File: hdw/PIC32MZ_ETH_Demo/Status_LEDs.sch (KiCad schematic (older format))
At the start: 30 parts

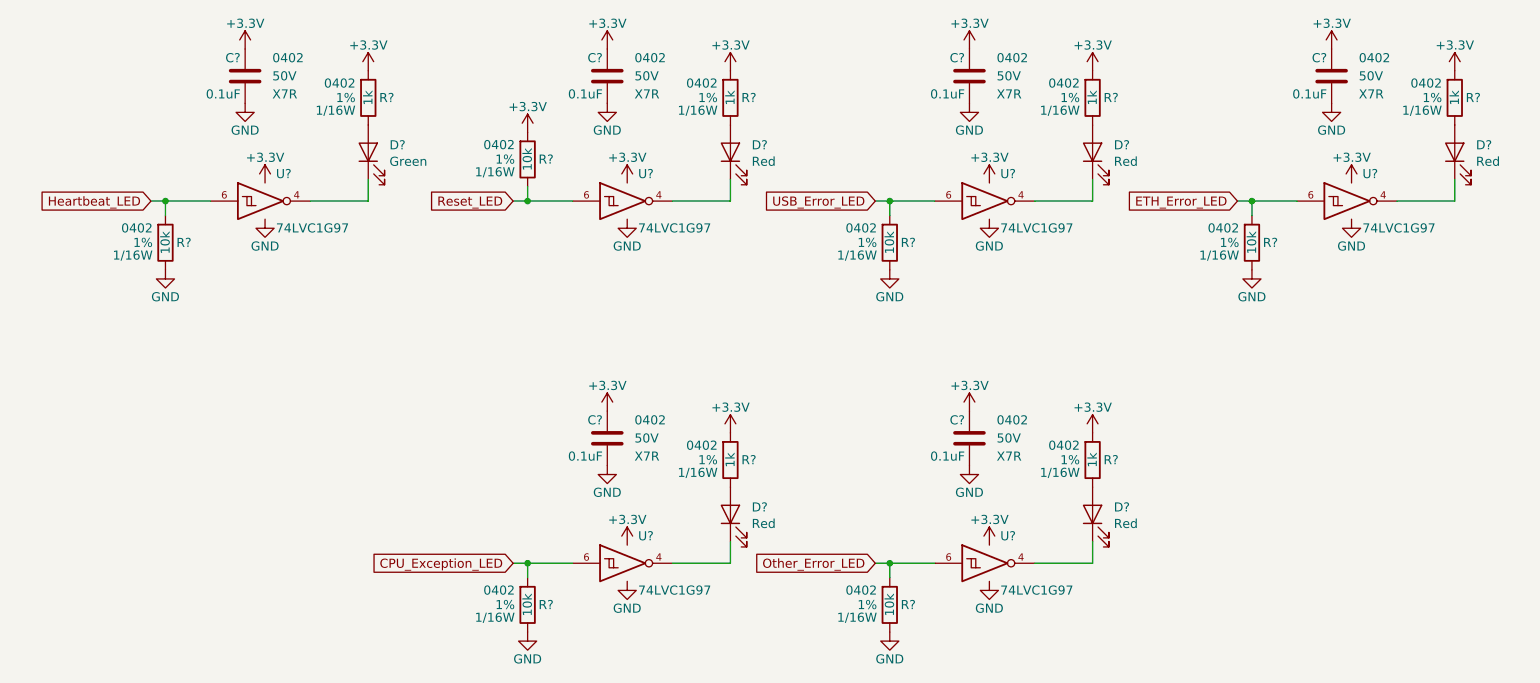
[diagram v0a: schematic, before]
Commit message: More schematic tweaks, followed PHY design guide
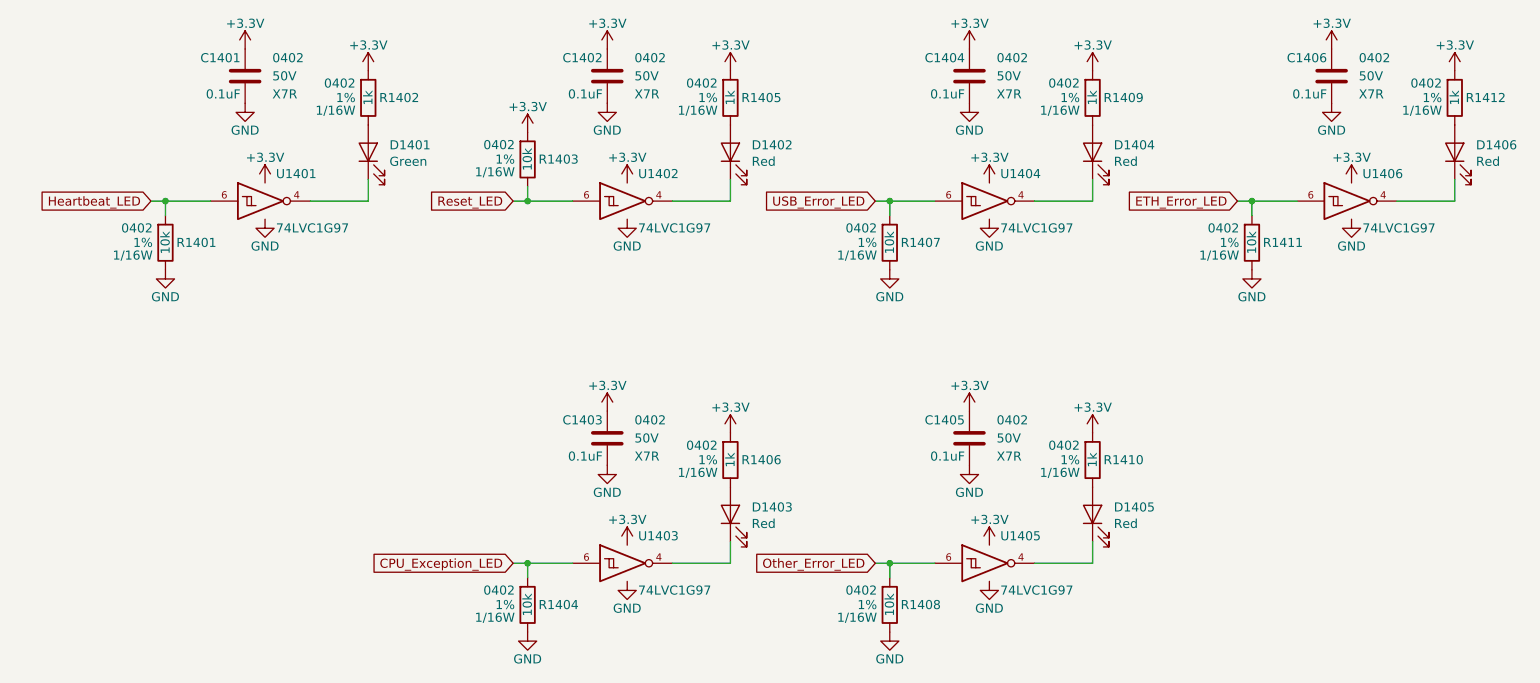
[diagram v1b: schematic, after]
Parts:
- gave numbers to parts that had none: 30

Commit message: Populated digi-key pn's
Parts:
- C1401, C1402, C1403, C1404, C1405, C1406: Digi-Key PN (none) -> 490-10701-1-ND
- D1401: footprint LEDs:LED_0603 -> LEDs:LED_0402; Digi-Key PN (none) -> 1497-1219-1-ND
- D1402, D1403, D1404, D1405, D1406: footprint LEDs:LED_0603 -> LEDs:LED_0402; Digi-Key PN (none) -> 1497-1174-1-ND
- R1401, R1403, R1404, R1407, R1408, R1411: Digi-Key PN (none) -> RMCF0402FT10K0CT-ND
- R1402, R1405, R1406, R1409, R1410, R1412: Digi-Key PN (none) -> 541-1.00KLCT-ND
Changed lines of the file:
@@
 F 2 "Capacitors_SMD:C_0402" H 2328 1380 50  0001 C CNN
 F 3 "" H 2315 1630 50  0001 C CNN
-F 4 "" H 2715 2030 60  0001 C CNN "Digi-Key PN"
+F 4 "490-10701-1-ND" H 2715 2030 60  0001 C CNN "Digi-Key PN"
 F 5 "0402" H 2140 1630 50  0000 R CNN "display_footprint"
 F 6 "50V" H 2140 1530 50  0000 R CNN "Voltage"
@@
 F 0 "D1401" V 3009 1833 50  0000 R CNN
 F 1 "Green" V 2918 1833 50  0000 R CNN
-F 2 "LEDs:LED_0603" H 2970 1950 50  0001 C CNN
+F 2 "LEDs:LED_0402" H 2970 1950 50  0001 C CNN
 F 3 "~" H 2970 1950 50  0001 C CNN
-F 4 "" H -2190 -4370 50  0001 C CNN "Digi-Key PN"
+F 4 "1497-1219-1-ND" H -2190 -4370 50  0001 C CNN "Digi-Key PN"
 	1    2970 1950
 	0    -1   -1   0
@@
 F 5 "1%" H 3040 1650 50  0000 L CNN "Tolerance"
 F 6 "1/16W" H 3040 1580 50  0000 L CNN "Wattage"
-F 7 "" H 3270 2050 60  0001 C CNN "Digi-Key PN"
+F 7 "541-1.00KLCT-ND" H 3270 2050 60  0001 C CNN "Digi-Key PN"
 	1    2970 1650
 	-1   0    0    -1
@@
 F 5 "1%" H 1920 2450 50  0000 L CNN "Tolerance"
 F 6 "1/16W" H 1920 2380 50  0000 L CNN "Wattage"
-F 7 "" H 1850 2450 50  0001 C CNN "Digi-Key PN"
+F 7 "RMCF0402FT10K0CT-ND" H 1850 2450 50  0001 C CNN "Digi-Key PN"
 	1    1850 2450
 	-1   0    0    -1
@@
 F 2 "Capacitors_SMD:C_0402" H 4328 1380 50  0001 C CNN
 F 3 "" H 4315 1630 50  0001 C CNN
-F 4 "" H 4715 2030 60  0001 C CNN "Digi-Key PN"
+F 4 "490-10701-1-ND" H 4715 2030 60  0001 C CNN "Digi-Key PN"
 F 5 "0402" H 4140 1630 50  0000 R CNN "display_footprint"
 F 6 "50V" H 4140 1530 50  0000 R CNN "Voltage"
@@
 F 0 "D1402" V 5009 1833 50  0000 R CNN
 F 1 "Red" V 4918 1833 50  0000 R CNN
-F 2 "LEDs:LED_0603" H 4970 1950 50  0001 C CNN
+F 2 "LEDs:LED_0402" H 4970 1950 50  0001 C CNN
 F 3 "~" H 4970 1950 50  0001 C CNN
-F 4 "" H 4970 1950 50  0001 C CNN "Digi-Key PN"
+F 4 "1497-1174-1-ND" H 4970 1950 50  0001 C CNN "Digi-Key PN"
 	1    4970 1950
 	0    -1   -1   0
@@
 F 5 "1%" H 5040 1650 50  0000 L CNN "Tolerance"
 F 6 "1/16W" H 5040 1580 50  0000 L CNN "Wattage"
-F 7 "" H 5270 2050 60  0001 C CNN "Digi-Key PN"
+F 7 "541-1.00KLCT-ND" H 5270 2050 60  0001 C CNN "Digi-Key PN"
 	1    4970 1650
 	-1   0    0    -1
@@
 F 5 "1%" H 3920 1990 50  0000 L CNN "Tolerance"
 F 6 "1/16W" H 3920 1920 50  0000 L CNN "Wattage"
-F 7 "" H 3850 1990 50  0001 C CNN "Digi-Key PN"
+F 7 "RMCF0402FT10K0CT-ND" H 3850 1990 50  0001 C CNN "Digi-Key PN"
 	1    3850 1990
 	-1   0    0    -1
@@
 F 2 "Capacitors_SMD:C_0402" H 6328 1380 50  0001 C CNN
 F 3 "" H 6315 1630 50  0001 C CNN
-F 4 "" H 6715 2030 60  0001 C CNN "Digi-Key PN"
+F 4 "490-10701-1-ND" H 6715 2030 60  0001 C CNN "Digi-Key PN"
 F 5 "0402" H 6140 1630 50  0000 R CNN "display_footprint"
 F 6 "50V" H 6140 1530 50  0000 R CNN "Voltage"
@@
 F 5 "1%" H 7040 1650 50  0000 L CNN "Tolerance"
 F 6 "1/16W" H 7040 1580 50  0000 L CNN "Wattage"
-F 7 "" H 7270 2050 60  0001 C CNN "Digi-Key PN"
+F 7 "541-1.00KLCT-ND" H 7270 2050 60  0001 C CNN "Digi-Key PN"
 	1    6970 1650
 	-1   0    0    -1
@@
 F 5 "1%" H 5920 2450 50  0000 L CNN "Tolerance"
 F 6 "1/16W" H 5920 2380 50  0000 L CNN "Wattage"
-F 7 "" H 5850 2450 50  0001 C CNN "Digi-Key PN"
+F 7 "RMCF0402FT10K0CT-ND" H 5850 2450 50  0001 C CNN "Digi-Key PN"
 	1    5850 2450
 	-1   0    0    -1
@@
 F 0 "D1404" V 7009 1833 50  0000 R CNN
 F 1 "Red" V 6918 1833 50  0000 R CNN
-F 2 "LEDs:LED_0603" H 6970 1950 50  0001 C CNN
+F 2 "LEDs:LED_0402" H 6970 1950 50  0001 C CNN
 F 3 "~" H 6970 1950 50  0001 C CNN
-F 4 "" H 6970 1950 50  0001 C CNN "Digi-Key PN"
+F 4 "1497-1174-1-ND" H 6970 1950 50  0001 C CNN "Digi-Key PN"
 	1    6970 1950
 	0    -1   -1   0
@@
 F 2 "Capacitors_SMD:C_0402" H 8328 1380 50  0001 C CNN
 F 3 "" H 8315 1630 50  0001 C CNN
-F 4 "" H 8715 2030 60  0001 C CNN "Digi-Key PN"
+F 4 "490-10701-1-ND" H 8715 2030 60  0001 C CNN "Digi-Key PN"
 F 5 "0402" H 8140 1630 50  0000 R CNN "display_footprint"
 F 6 "50V" H 8140 1530 50  0000 R CNN "Voltage"
@@
 F 5 "1%" H 9040 1650 50  0000 L CNN "Tolerance"
 F 6 "1/16W" H 9040 1580 50  0000 L CNN "Wattage"
-F 7 "" H 9270 2050 60  0001 C CNN "Digi-Key PN"
+F 7 "541-1.00KLCT-ND" H 9270 2050 60  0001 C CNN "Digi-Key PN"
 	1    8970 1650
 	-1   0    0    -1
@@
 F 5 "1%" H 7920 2450 50  0000 L CNN "Tolerance"
 F 6 "1/16W" H 7920 2380 50  0000 L CNN "Wattage"
-F 7 "" H 7850 2450 50  0001 C CNN "Digi-Key PN"
+F 7 "RMCF0402FT10K0CT-ND" H 7850 2450 50  0001 C CNN "Digi-Key PN"
 	1    7850 2450
 	-1   0    0    -1
@@
 F 0 "D1406" V 9009 1833 50  0000 R CNN
 F 1 "Red" V 8918 1833 50  0000 R CNN
-F 2 "LEDs:LED_0603" H 8970 1950 50  0001 C CNN
+F 2 "LEDs:LED_0402" H 8970 1950 50  0001 C CNN
 F 3 "~" H 8970 1950 50  0001 C CNN
-F 4 "" H 8970 1950 50  0001 C CNN "Digi-Key PN"
+F 4 "1497-1174-1-ND" H 8970 1950 50  0001 C CNN "Digi-Key PN"
 	1    8970 1950
 	0    -1   -1   0
@@
 F 2 "Capacitors_SMD:C_0402" H 6328 3380 50  0001 C CNN
 F 3 "" H 6315 3630 50  0001 C CNN
-F 4 "" H 6715 4030 60  0001 C CNN "Digi-Key PN"
+F 4 "490-10701-1-ND" H 6715 4030 60  0001 C CNN "Digi-Key PN"
 F 5 "0402" H 6140 3630 50  0000 R CNN "display_footprint"
 F 6 "50V" H 6140 3530 50  0000 R CNN "Voltage"
@@
 F 5 "1%" H 7040 3650 50  0000 L CNN "Tolerance"
 F 6 "1/16W" H 7040 3580 50  0000 L CNN "Wattage"
-F 7 "" H 7270 4050 60  0001 C CNN "Digi-Key PN"
+F 7 "541-1.00KLCT-ND" H 7270 4050 60  0001 C CNN "Digi-Key PN"
 	1    6970 3650
 	-1   0    0    -1
@@
 F 5 "1%" H 5920 4450 50  0000 L CNN "Tolerance"
 F 6 "1/16W" H 5920 4380 50  0000 L CNN "Wattage"
-F 7 "" H 5850 4450 50  0001 C CNN "Digi-Key PN"
+F 7 "RMCF0402FT10K0CT-ND" H 5850 4450 50  0001 C CNN "Digi-Key PN"
 	1    5850 4450
 	-1   0    0    -1
@@
 F 0 "D1405" V 7009 3833 50  0000 R CNN
 F 1 "Red" V 6918 3833 50  0000 R CNN
-F 2 "LEDs:LED_0603" H 6970 3950 50  0001 C CNN
+F 2 "LEDs:LED_0402" H 6970 3950 50  0001 C CNN
 F 3 "~" H 6970 3950 50  0001 C CNN
-F 4 "" H 6970 3950 50  0001 C CNN "Digi-Key PN"
+F 4 "1497-1174-1-ND" H 6970 3950 50  0001 C CNN "Digi-Key PN"
 	1    6970 3950
 	0    -1   -1   0
@@
 F 2 "Capacitors_SMD:C_0402" H 4328 3380 50  0001 C CNN
 F 3 "" H 4315 3630 50  0001 C CNN
-F 4 "" H 4715 4030 60  0001 C CNN "Digi-Key PN"
+F 4 "490-10701-1-ND" H 4715 4030 60  0001 C CNN "Digi-Key PN"
 F 5 "0402" H 4140 3630 50  0000 R CNN "display_footprint"
 F 6 "50V" H 4140 3530 50  0000 R CNN "Voltage"
@@
 F 5 "1%" H 5040 3650 50  0000 L CNN "Tolerance"
 F 6 "1/16W" H 5040 3580 50  0000 L CNN "Wattage"
-F 7 "" H 5270 4050 60  0001 C CNN "Digi-Key PN"
+F 7 "541-1.00KLCT-ND" H 5270 4050 60  0001 C CNN "Digi-Key PN"
 	1    4970 3650
 	-1   0    0    -1
@@
 F 5 "1%" H 3920 4450 50  0000 L CNN "Tolerance"
 F 6 "1/16W" H 3920 4380 50  0000 L CNN "Wattage"
-F 7 "" H 3850 4450 50  0001 C CNN "Digi-Key PN"
+F 7 "RMCF0402FT10K0CT-ND" H 3850 4450 50  0001 C CNN "Digi-Key PN"
 	1    3850 4450
 	-1   0    0    -1
@@
 F 0 "D1403" V 5009 3833 50  0000 R CNN
 F 1 "Red" V 4918 3833 50  0000 R CNN
-F 2 "LEDs:LED_0603" H 4970 3950 50  0001 C CNN
+F 2 "LEDs:LED_0402" H 4970 3950 50  0001 C CNN
 F 3 "~" H 4970 3950 50  0001 C CNN
-F 4 "" H 4970 3950 50  0001 C CNN "Digi-Key PN"
+F 4 "1497-1174-1-ND" H 4970 3950 50  0001 C CNN "Digi-Key PN"
 	1    4970 3950
 	0    -1   -1   0
